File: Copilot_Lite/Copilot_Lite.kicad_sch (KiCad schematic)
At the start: 14 parts, among them J2 JACK_POWER_IN, J3 USB_POWER_IN, J4 USB_PC, J6 5V_ENABLE, J7 SERIAL_AND_GPIO, J8 JACK_POWER_OUT, J9 USB_POWER_OUT

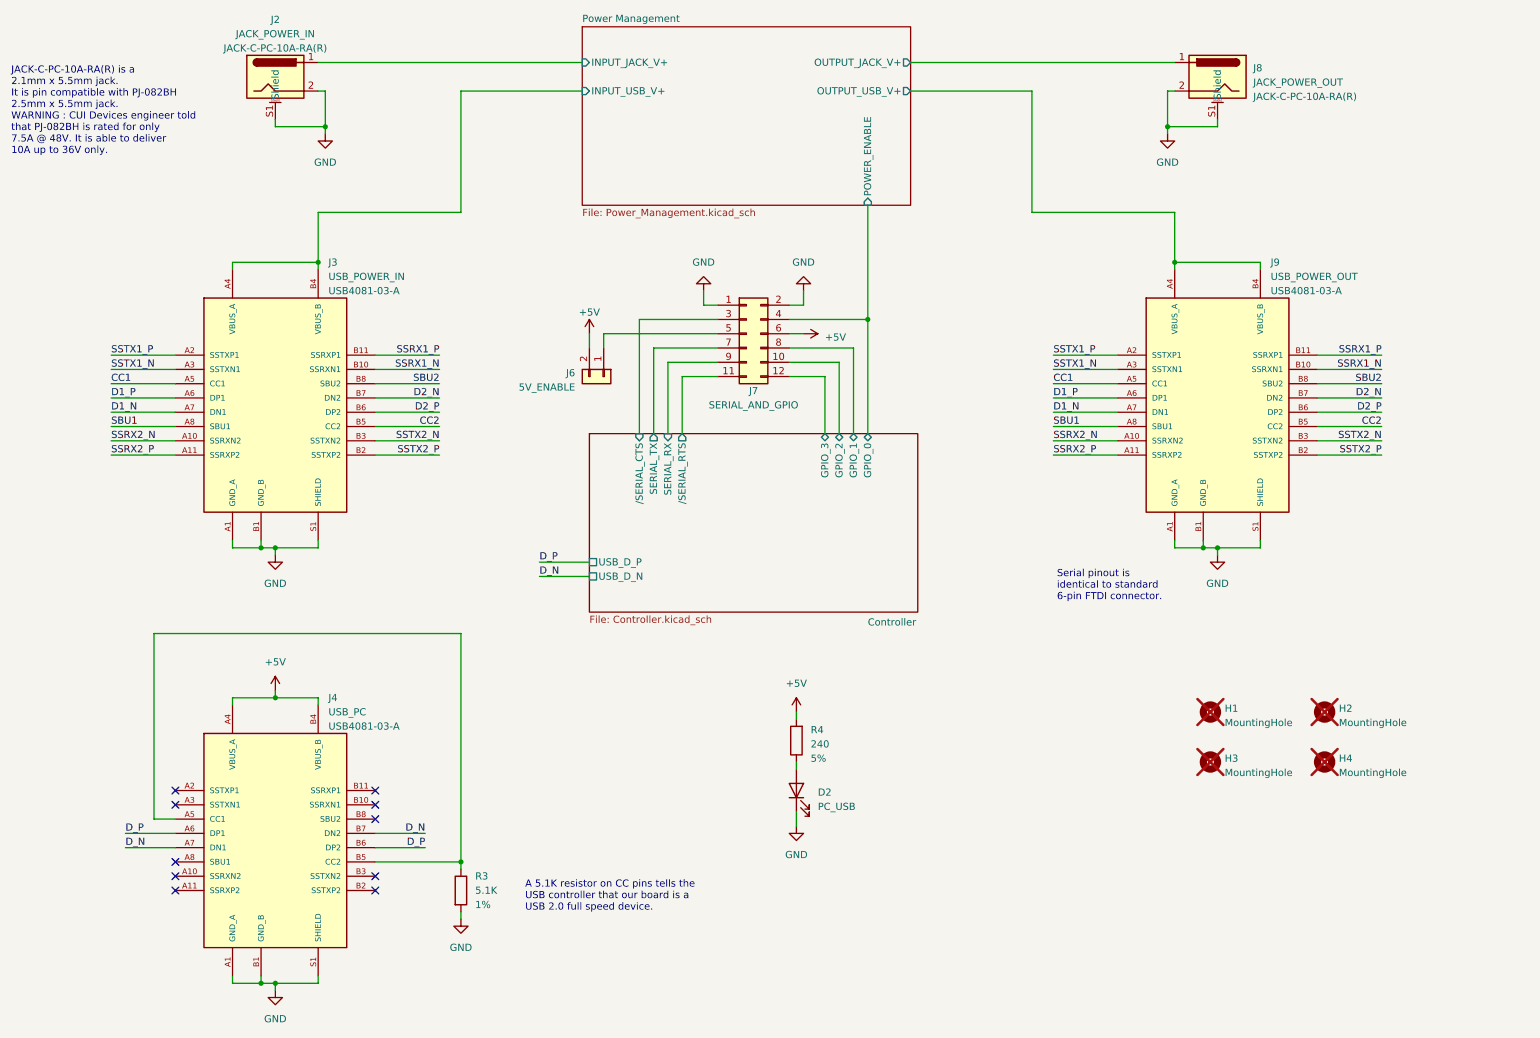
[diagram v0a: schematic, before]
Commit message: lite: Crossed the USB-C superspeed pairs and SBU signals.
The superspeed pairs and SBU signals of an USB-C cable are crossed.
As Copilot requires two cables, it uncrosses the signals.
That's why Copilot needs to cross again such signals.

Signed-off-by: Adrien Ricciardi <aricciardi@baylibre.com>
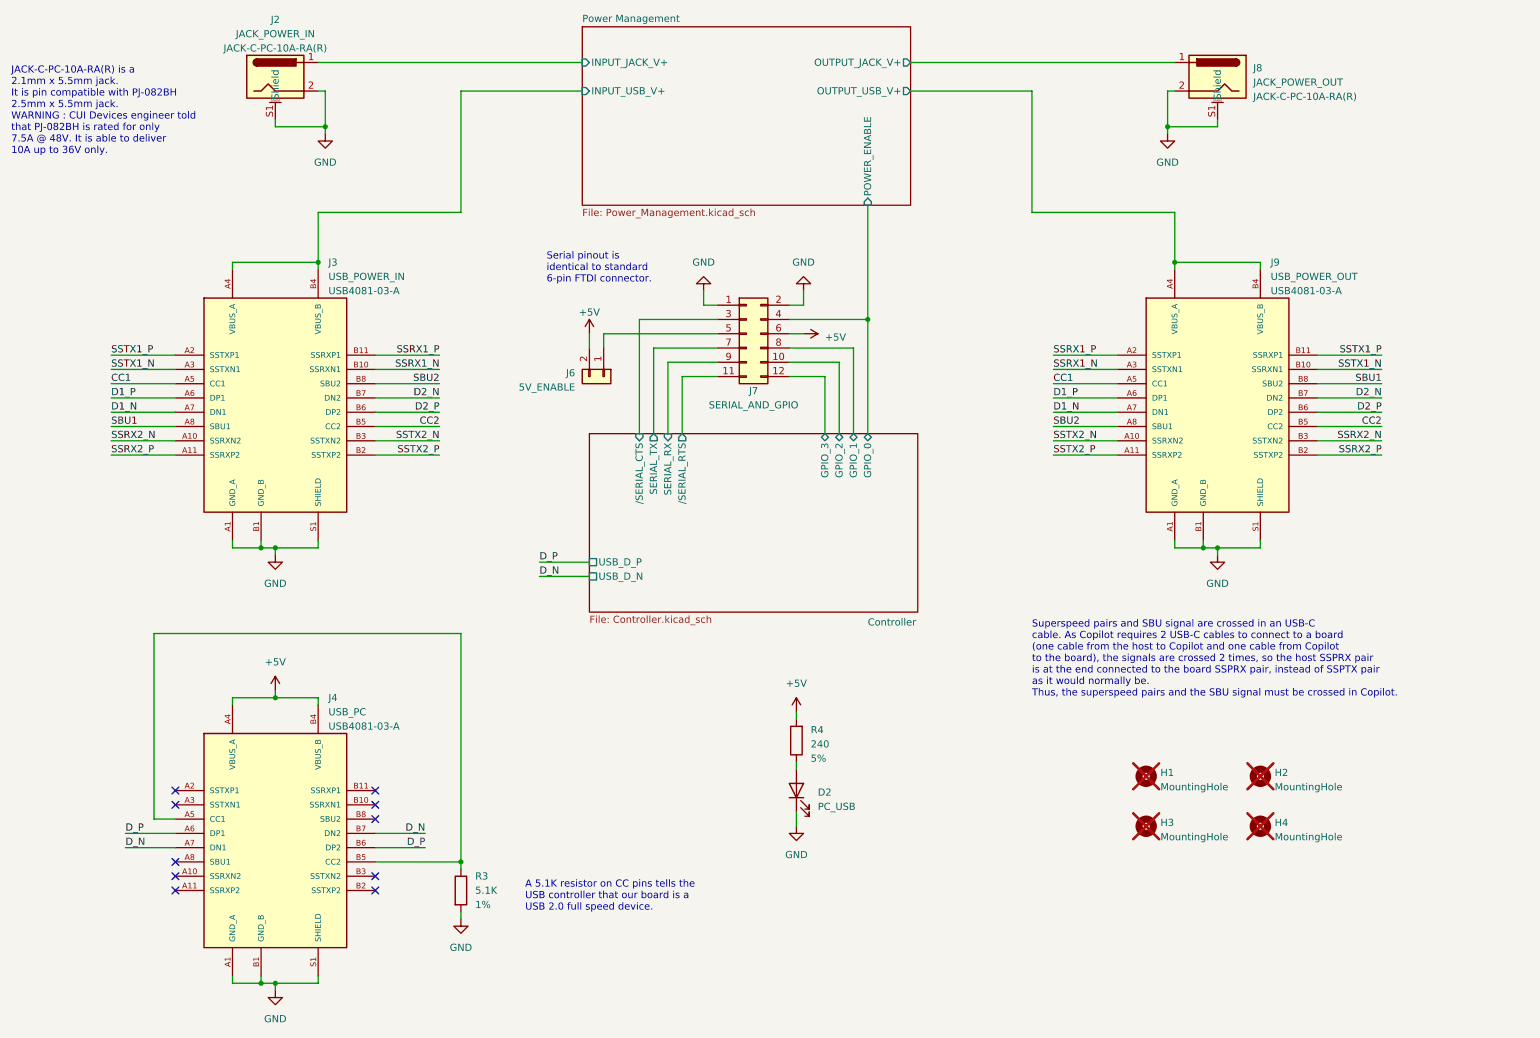
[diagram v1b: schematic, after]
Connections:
- net SBU1: now also J9.B8 (SBU2); no longer J9.A8 (SBU1)
- net SBU2: now also J9.A8 (SBU1); no longer J9.B8 (SBU2)
- net SSRX1_N: now also J9.A3 (SSTXN1); no longer J9.B10 (SSRXN1)
- net SSRX1_P: now also J9.A2 (SSTXP1); no longer J9.B11 (SSRXP1)
- net SSRX2_N: now also J9.B3 (SSTXN2); no longer J9.A10 (SSRXN2)
- net SSRX2_P: now also J9.B2 (SSTXP2); no longer J9.A11 (SSRXP2)
- net SSTX1_N: now also J9.B10 (SSRXN1); no longer J9.A3 (SSTXN1)
- net SSTX1_P: now also J9.B11 (SSRXP1); no longer J9.A2 (SSTXP1)
- net SSTX2_N: now also J9.A10 (SSRXN2); no longer J9.B3 (SSTXN2)
- net SSTX2_P: now also J9.A11 (SSRXP2); no longer J9.B2 (SSTXP2)
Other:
- note added: "Superspeed pairs and SBU signal are crossed in an USB-C cable. As Copilot requires 2 USB-C cables to connect to a board (one cable from the host to Copilot and one cable from Copilot to the board), the signals are crossed 2 times, so the host SSPRX pair is at the end connected to the board SSPRX pair, instead of SSPTX pair as it would normally be. Thus, the superspeed pairs and the SBU signal mus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"
- moved on the sheet: H1, H2, H3, H4
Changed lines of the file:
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@@
+    (effects (font (size 1.27 1.27)) (justify left bottom))
+  )
+  (text "Superspeed pairs and SBU signal are crossed in an USB-C\ncable. As Copilot requires 2 USB-C cables to connect to a board\n(one cable from the host to Copilot and one cable from Copilot\nto the board), the signals are crossed 2 times, so the host SSPRX pair\nis at the end connected to the board SSPRX pair, instead of SSPTX pair\nas it would normally be.\nThus, the superspeed pairs and the SBU signal must be crossed in Copilot."
+    (at 196.85 137.16 0)
     (effects (font (size 1.27 1.27)) (justify left bottom))
   )
   (text "Serial pinout is\nidentical to standard\n6-pin FTDI connector."
-    (at 201.295 120.015 0)
-    (effects (font (size 1.27 1.27)) (justify left bottom))
-  )
-  (label "SSRX1_P" (at 259.08 76.2 180) (fields_autoplaced)
+    (at 110.49 63.5 0)
+    (effects (font (size 1.27 1.27)) (justify left bottom))
+  )
+  (label "SSTX1_P" (at 259.08 76.2 180) (fields_autoplaced)
     (effects (font (size 1.27 1.27)) (justify right bottom))
   )
@@
     (effects (font (size 1.27 1.27)) (justify right bottom))
   )
-  (label "SSRX2_P" (at 200.66 93.98 0) (fields_autoplaced)
+  (label "SSTX2_P" (at 200.66 93.98 0) (fields_autoplaced)
     (effects (font (size 1.27 1.27)) (justify left bottom))
   )
@@
     (effects (font (size 1.27 1.27)) (justify left bottom))
   )
-  (label "SSTX1_P" (at 200.66 76.2 0) (fields_autoplaced)
+  (label "SSRX1_P" (at 200.66 76.2 0) (fields_autoplaced)
     (effects (font (size 1.27 1.27)) (justify left bottom))
   )
@@
     (effects (font (size 1.27 1.27)) (justify left bottom))
   )
-  (label "SBU1" (at 200.66 88.9 0) (fields_autoplaced)
-    (effects (font (size 1.27 1.27)) (justify left bottom))
-  )
-  (label "SSTX2_N" (at 259.08 91.44 180) (fields_autoplaced)
+  (label "SBU2" (at 200.66 88.9 0) (fields_autoplaced)
+    (effects (font (size 1.27 1.27)) (justify left bottom))
+  )
+  (label "SSRX2_N" (at 259.08 91.44 180) (fields_autoplaced)
     (effects (font (size 1.27 1.27)) (justify right bottom))
   )
@@
     (effects (font (size 1.27 1.27)) (justify left bottom))
   )
-  (label "SSTX2_P" (at 259.08 93.98 180) (fields_autoplaced)
+  (label "SSRX2_P" (at 259.08 93.98 180) (fields_autoplaced)
     (effects (font (size 1.27 1.27)) (justify right bottom))
   )
@@
     (effects (font (size 1.27 1.27)) (justify right bottom))
   )
-  (label "SBU2" (at 259.08 81.28 180) (fields_autoplaced)
+  (label "SBU1" (at 259.08 81.28 180) (fields_autoplaced)
     (effects (font (size 1.27 1.27)) (justify right bottom))
   )
@@
     (effects (font (size 1.27 1.27)) (justify left bottom))
   )
-  (label "SSRX2_N" (at 200.66 91.44 0) (fields_autoplaced)
+  (label "SSTX2_N" (at 200.66 91.44 0) (fields_autoplaced)
     (effects (font (size 1.27 1.27)) (justify left bottom))
   )
@@
     (effects (font (size 1.27 1.27)) (justify right bottom))
   )
-  (label "SSTX1_N" (at 200.66 78.74 0) (fields_autoplaced)
-    (effects (font (size 1.27 1.27)) (justify left bottom))
-  )
-  (label "SSRX1_N" (at 259.08 78.74 180) (fields_autoplaced)
+  (label "SSRX1_N" (at 200.66 78.74 0) (fields_autoplaced)
+    (effects (font (size 1.27 1.27)) (justify left bottom))
+  )
+  (label "SSTX1_N" (at 259.08 78.74 180) (fields_autoplaced)
     (effects (font (size 1.27 1.27)) (justify right bottom))
   )
@@
     )
   )
-  (symbol (lib_id "Mechanical:MountingHole") (at 228.6 139.7 0) (unit 1)
+  (symbol (lib_id "Mechanical:MountingHole") (at 217.17 151.13 0) (unit 1)
     (in_bom no) (on_board yes) (dnp yes) (fields_autoplaced)
-    (property "Reference" "H1" (at 231.14 139.065 0)
-      (effects (font (size 1.27 1.27)) (justify left))
-    )
-    (property "Value" "MountingHole" (at 231.14 141.605 0)
-      (effects (font (size 1.27 1.27)) (justify left))
-    )
-    (property "Footprint" "MountingHole:MountingHole_2.7mm" (at 228.6 139.7 0)
-      (effects (font (size 1.27 1.27)) hide)
-    )
-    (property "Datasheet" "~" (at 228.6 139.7 0)
+    (property "Reference" "H1" (at 219.71 150.495 0)
+      (effects (font (size 1.27 1.27)) (justify left))
+    )
+    (property "Value" "MountingHole" (at 219.71 153.035 0)
+      (effects (font (size 1.27 1.27)) (justify left))
+    )
+    (property "Footprint" "MountingHole:MountingHole_2.7mm" (at 217.17 151.13 0)
+      (effects (font (size 1.27 1.27)) hide)
+    )
+    (property "Datasheet" "~" (at 217.17 151.13 0)
       (effects (font (size 1.27 1.27)) hide)
     )
@@
     )
   )
-  (symbol (lib_id "Mechanical:MountingHole") (at 228.6 148.59 0) (unit 1)
+  (symbol (lib_id "Mechanical:MountingHole") (at 217.17 160.02 0) (unit 1)
     (in_bom no) (on_board yes) (dnp yes) (fields_autoplaced)
-    (property "Reference" "H3" (at 231.14 147.955 0)
-      (effects (font (size 1.27 1.27)) (justify left))
-    )
-    (property "Value" "MountingHole" (at 231.14 150.495 0)
-      (effects (font (size 1.27 1.27)) (justify left))
-    )
-    (property "Footprint" "MountingHole:MountingHole_2.7mm" (at 228.6 148.59 0)
-      (effects (font (size 1.27 1.27)) hide)
-    )
-    (property "Datasheet" "~" (at 228.6 148.59 0)
+    (property "Reference" "H3" (at 219.71 159.385 0)
+      (effects (font (size 1.27 1.27)) (justify left))
+    )
+    (property "Value" "MountingHole" (at 219.71 161.925 0)
+      (effects (font (size 1.27 1.27)) (justify left))
+    )
+    (property "Footprint" "MountingHole:MountingHole_2.7mm" (at 217.17 160.02 0)
+      (effects (font (size 1.27 1.27)) hide)
+    )
+    (property "Datasheet" "~" (at 217.17 160.02 0)
       (effects (font (size 1.27 1.27)) hide)
     )
@@
     )
   )
-  (symbol (lib_id "Mechanical:MountingHole") (at 248.92 148.59 0) (unit 1)
+  (symbol (lib_id "Mechanical:MountingHole") (at 237.49 160.02 0) (unit 1)
     (in_bom no) (on_board yes) (dnp yes) (fields_autoplaced)
-    (property "Reference" "H4" (at 251.46 147.955 0)
-      (effects (font (size 1.27 1.27)) (justify left))
-    )
-    (property "Value" "MountingHole" (at 251.46 150.495 0)
-      (effects (font (size 1.27 1.27)) (justify left))
-    )
-    (property "Footprint" "MountingHole:MountingHole_2.7mm" (at 248.92 148.59 0)
-      (effects (font (size 1.27 1.27)) hide)
-    )
-    (property "Datasheet" "~" (at 248.92 148.59 0)
+    (property "Reference" "H4" (at 240.03 159.385 0)
+      (effects (font (size 1.27 1.27)) (justify left))
+    )
+    (property "Value" "MountingHole" (at 240.03 161.925 0)
+      (effects (font (size 1.27 1.27)) (justify left))
+    )
+    (property "Footprint" "MountingHole:MountingHole_2.7mm" (at 237.49 160.02 0)
+      (effects (font (size 1.27 1.27)) hide)
+    )
+    (property "Datasheet" "~" (at 237.49 160.02 0)
       (effects (font (size 1.27 1.27)) hide)
     )
@@
     )
   )
-  (symbol (lib_id "Mechanical:MountingHole") (at 248.92 139.7 0) (unit 1)
+  (symbol (lib_id "Mechanical:MountingHole") (at 237.49 151.13 0) (unit 1)
     (in_bom no) (on_board yes) (dnp yes) (fields_autoplaced)
-    (property "Reference" "H2" (at 251.46 139.065 0)
-      (effects (font (size 1.27 1.27)) (justify left))
-    )
-    (property "Value" "MountingHole" (at 251.46 141.605 0)
-      (effects (font (size 1.27 1.27)) (justify left))
-    )
-    (property "Footprint" "MountingHole:MountingHole_2.7mm" (at 248.92 139.7 0)
-      (effects (font (size 1.27 1.27)) hide)
-    )
-    (property "Datasheet" "~" (at 248.92 139.7 0)
-      (effects (font (size 1.27 1.27)) hide)
-    )
+    (property "Reference" "H2" (at 240.03 150.495 0)
+      (effects (font (size 1.27 1.27)) (justify left))
+    )
+    (property "Value" "MountingHole" (at 240.03 153.035 0)
+      (effects (font (size 1.27 1.27)) (justify left))
+    )
+    (property "Footprint" "MountingHole:MountingHole_2.7mm" (at 237.49 151.13 0)
+      (effects (font (size 1.27 1.27)) hide)
+    )
+    (property "Datasheet" "~" (at 237.49 151.13 0)
+      (effects (font (size 1.27 1.27)) hide)
+    )

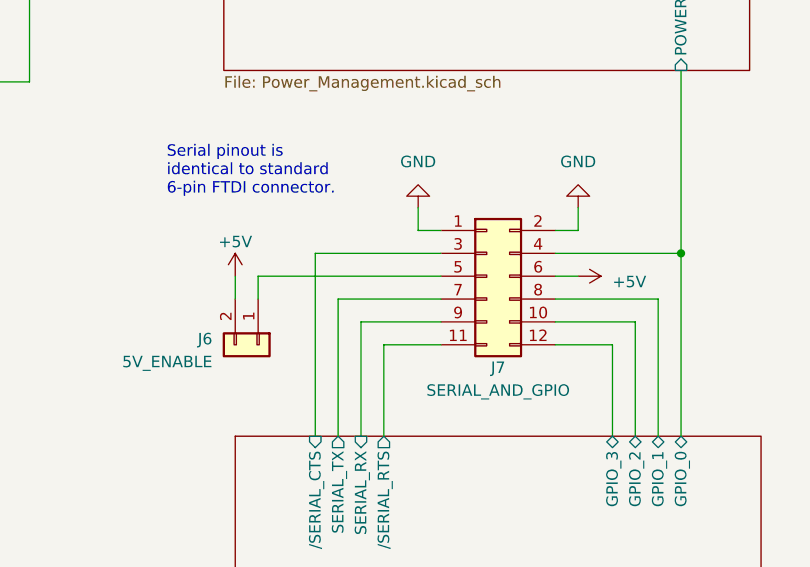
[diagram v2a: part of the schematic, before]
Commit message: lite: Swapped UART and GPIO pin header rows in both schematic and PCB.
This allows to more easily use a mezzanine board.

It is now possible to solder a single row vertical pin header on the row
that is located inside the PCB and a right-angled single row pin header on
the row facing the PCB edge to still get access to the UART pins.
This way, the GPIOs can reach the mezzanine board and there is no need to
"forward" the UART signals to the mezzanine board.

Signed-off-by: Adrien Ricciardi <aricciardi@baylibre.com>
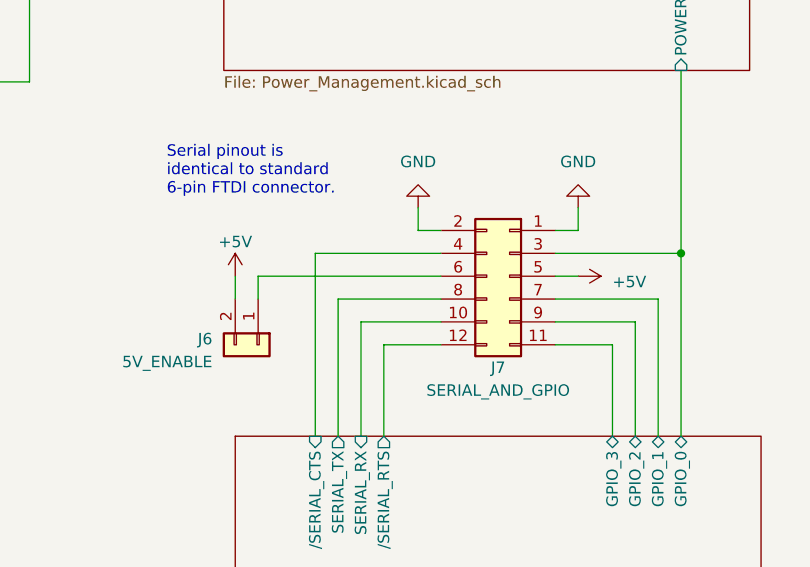
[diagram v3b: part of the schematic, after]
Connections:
- net +5V: now also J7.5 (Pin_5); no longer J7.6 (Pin_6)
- net Controller/GPIO_0: now also J7.3 (Pin_3); no longer J7.4 (Pin_4)
- net Controller/GPIO_1: now also J7.7 (Pin_7); no longer J7.8 (Pin_8)
- net Controller/GPIO_2: now also J7.9 (Pin_9); no longer J7.10 (Pin_10)
- net Controller/GPIO_3: now also J7.11 (Pin_11); no longer J7.12 (Pin_12)
- net Controller/SERIAL_RX: now also J7.10 (Pin_10); no longer J7.9 (Pin_9)
- net Controller/SERIAL_TX: now also J7.8 (Pin_8); no longer J7.7 (Pin_7)
- net Controller//SERIAL_CTS: now also J7.4 (Pin_4); no longer J7.3 (Pin_3)
- net Controller//SERIAL_RTS: now also J7.12 (Pin_12); no longer J7.11 (Pin_11)
- net at J6.1 (Pin_1): now also J7.6 (Pin_6); no longer J7.5 (Pin_5)
